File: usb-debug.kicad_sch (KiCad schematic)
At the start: 87 parts, among them IC1 NCP380LSNAJAAT1G, IC15 TPS7A0518PDBVT, IC3 NCP380LSNAJAAT1G, IC7 HD3SS3220, J11 632723300011, T6 BSS138APW, T7 BSS138APW, T9 BSS138APW, U8 74LVC1G07GV

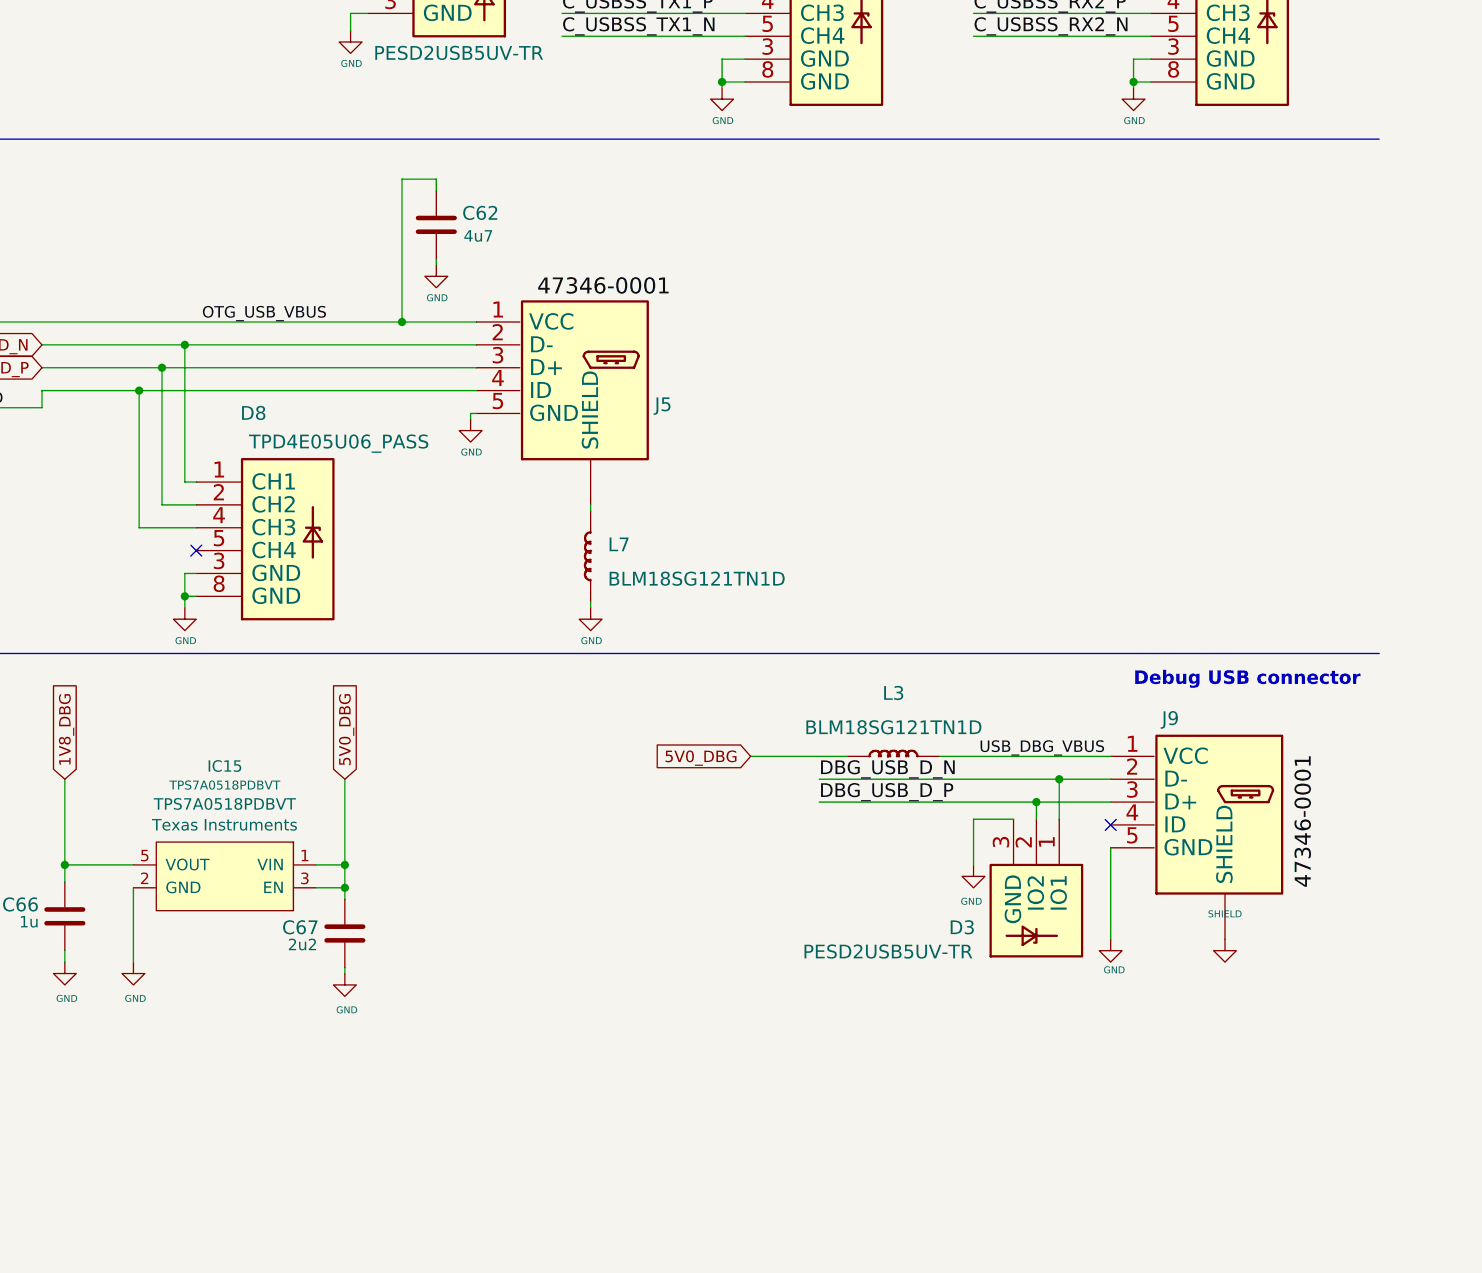
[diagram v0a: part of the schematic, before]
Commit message: WIP: Re-design base board
1. change to more common connector from JLC
2. add WIFI M.2 Key-E connector
3. add USB Hub which contained in nVidia version board
4. change DC connecotor to XT30
5. change USB Mico-B to USB Type C
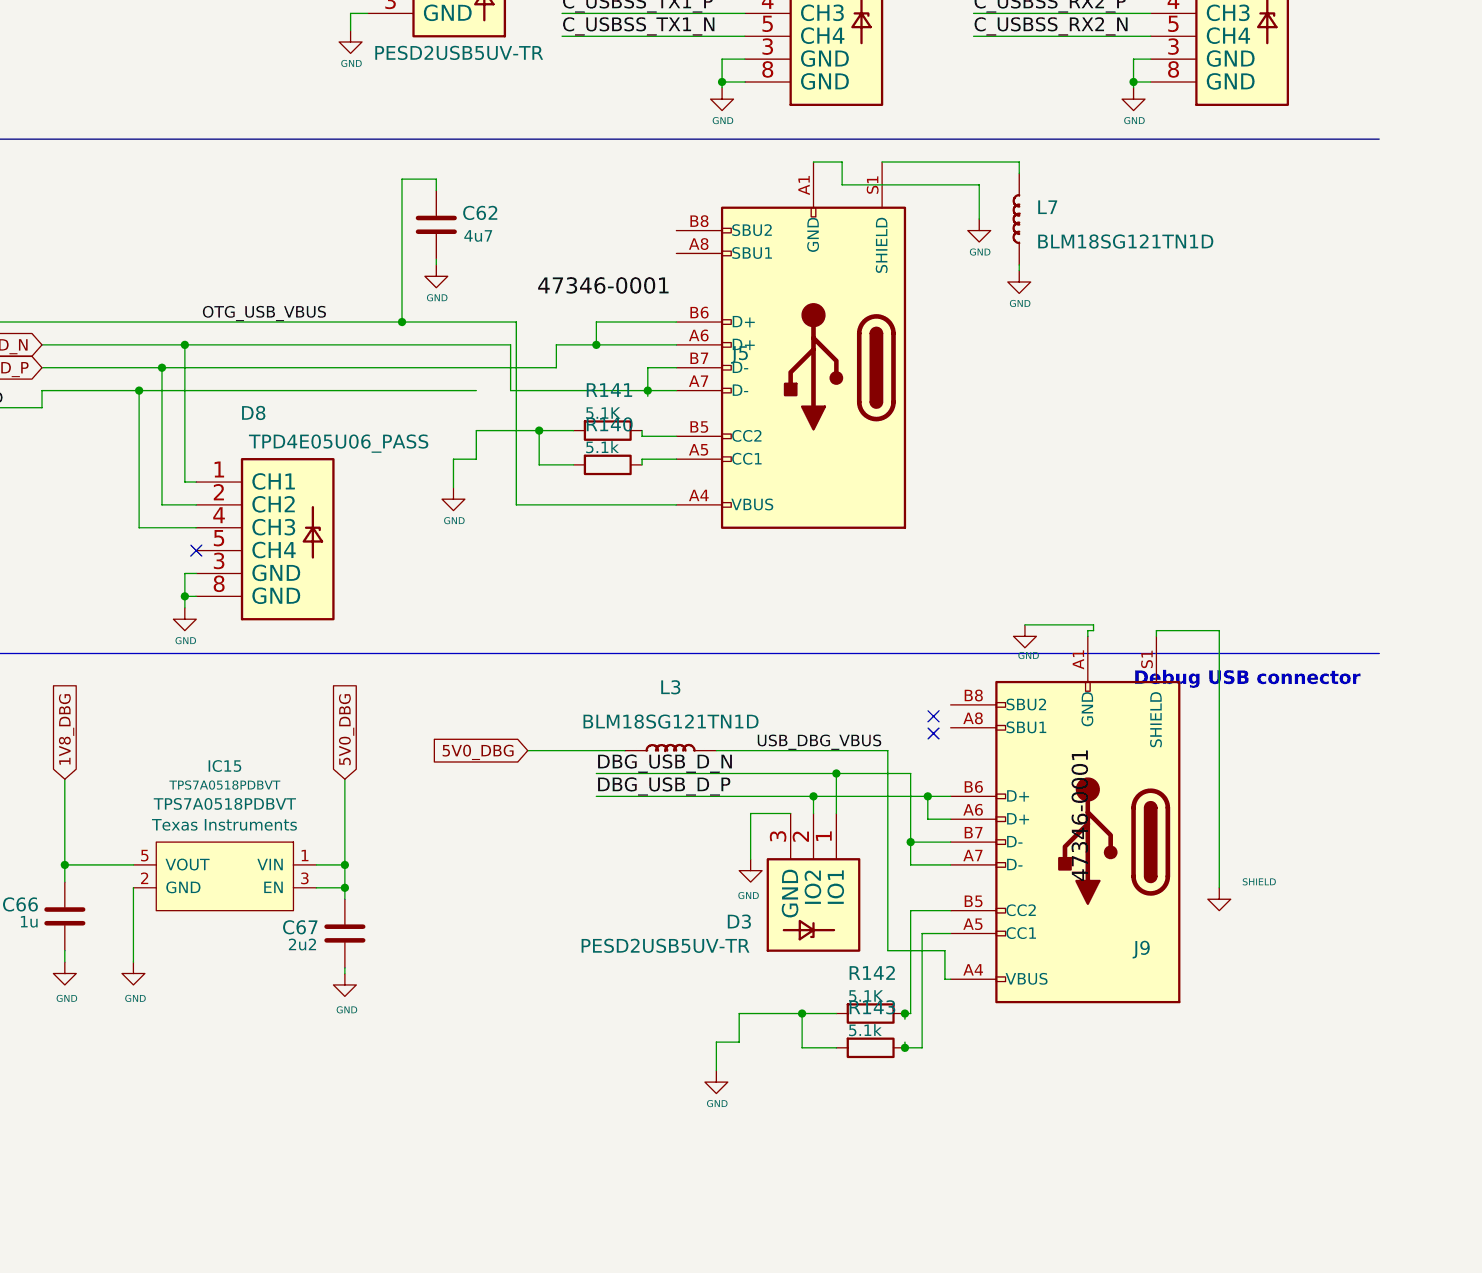
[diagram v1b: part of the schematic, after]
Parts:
- added R140, R141, R142, R143: R_10k_0402, jetson-nano-baseboard-footprints:0402-res, symbol jetson-nano-baseboard:R_10k_0402
- J5, J9: footprint jetson-nano-baseboard-footprints:CON-Molex-047346-0001 -> JLC_Footprint:JLC_USB-C-SMD_KH-TYPE-C-16P; symbol jetson-nano-baseboard:Micro_USB_B -> Connector:USB_C_Receptacle_USB2.0
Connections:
- net DBG_USB_D_N: now also J9.A7 (D-), J9.B7 (D-); no longer J9.2 (D-)
- net DBG_USB_D_P: now also J9.A6 (D+), J9.B6 (D+); no longer J9.3 (D+)
- net GND: now also J5.A1 (GND), J5.A12 (GND), J5.B1 (GND), J5.B12 (GND), J9.A1 (GND), J9.A12 (GND), J9.B1 (GND), J9.B12 (GND), J9.S1 (SHIELD), R140.2, R141.2, R142.2, R143.2; no longer J5.5 (GND), J9.5 (GND), J9.S (SHIELD)
- net OTG_USB_D_N: now also J5.A7 (D-), J5.B7 (D-); no longer J5.2 (D-)
- net OTG_USB_D_P: now also J5.A6 (D+), J5.B6 (D+); no longer J5.3 (D+)
- net OTG_USB_ID: no longer J5.4 (ID)
- net OTG_USB_VBUS: now also J5.A4 (VBUS), J5.A9 (VBUS), J5.B4 (VBUS), J5.B9 (VBUS); no longer J5.1 (VCC)
- net USB_DBG_VBUS: now also J9.A4 (VBUS), J9.A9 (VBUS), J9.B4 (VBUS), J9.B9 (VBUS); no longer J9.1 (VCC)
- net at L7.2 (P): now also J5.S1 (SHIELD); no longer J5.S (SHIELD)
- new net: J5.A5 (CC1), R140.1
- new net: J5.B5 (CC2), R141.1
- new net: J9.A5 (CC1), R143.1
- new net: J9.B5 (CC2), R142.1
- no-connect marks 17 -> 18
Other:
- moved on the sheet: D3, L3, L7
